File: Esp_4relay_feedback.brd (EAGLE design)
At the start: 150 x 100 mm, 93 parts, among them IC1 LM1117MP-3.3, IC2 NE555, IC4 7805TV, K1 G5LE, K2 G5LE, K3 G5LE, K4 G5LE, K5 G5LE, K6 G5LE, K7 G5LE, K8 G5LE, Q1 16MHz, Q11 BC450, Q2 BC547, Q3 BC547, Q4 BC547, Q5 BC547, Q6 BC547, Q7 BC547, Q8 BC547, Q9 BC547, T1 2N7000, T2 2N7000, U2 ATMEGA328P_PDIP

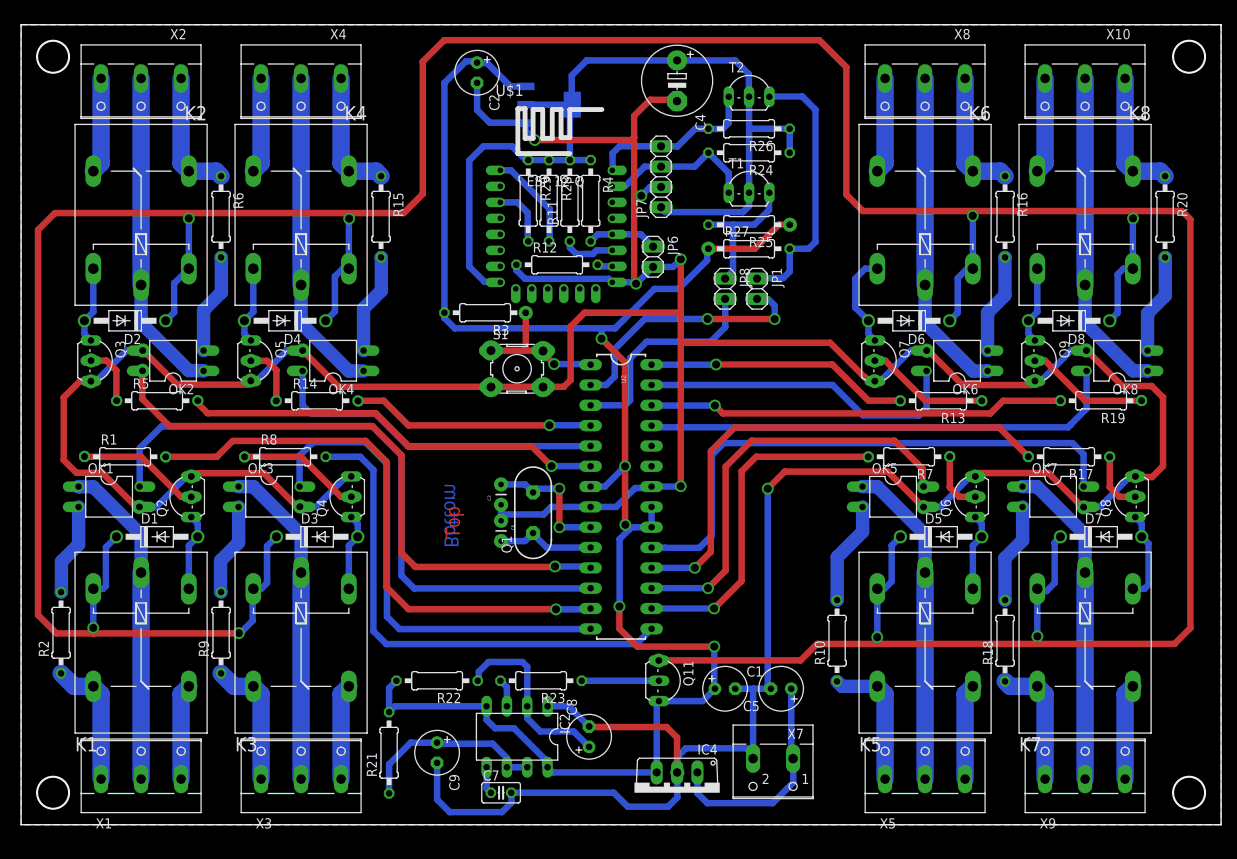
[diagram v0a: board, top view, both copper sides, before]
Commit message: schematic change
feedback circuit connection changed
added tip127 to control relay power supply.
made separate supply for relay and controller.
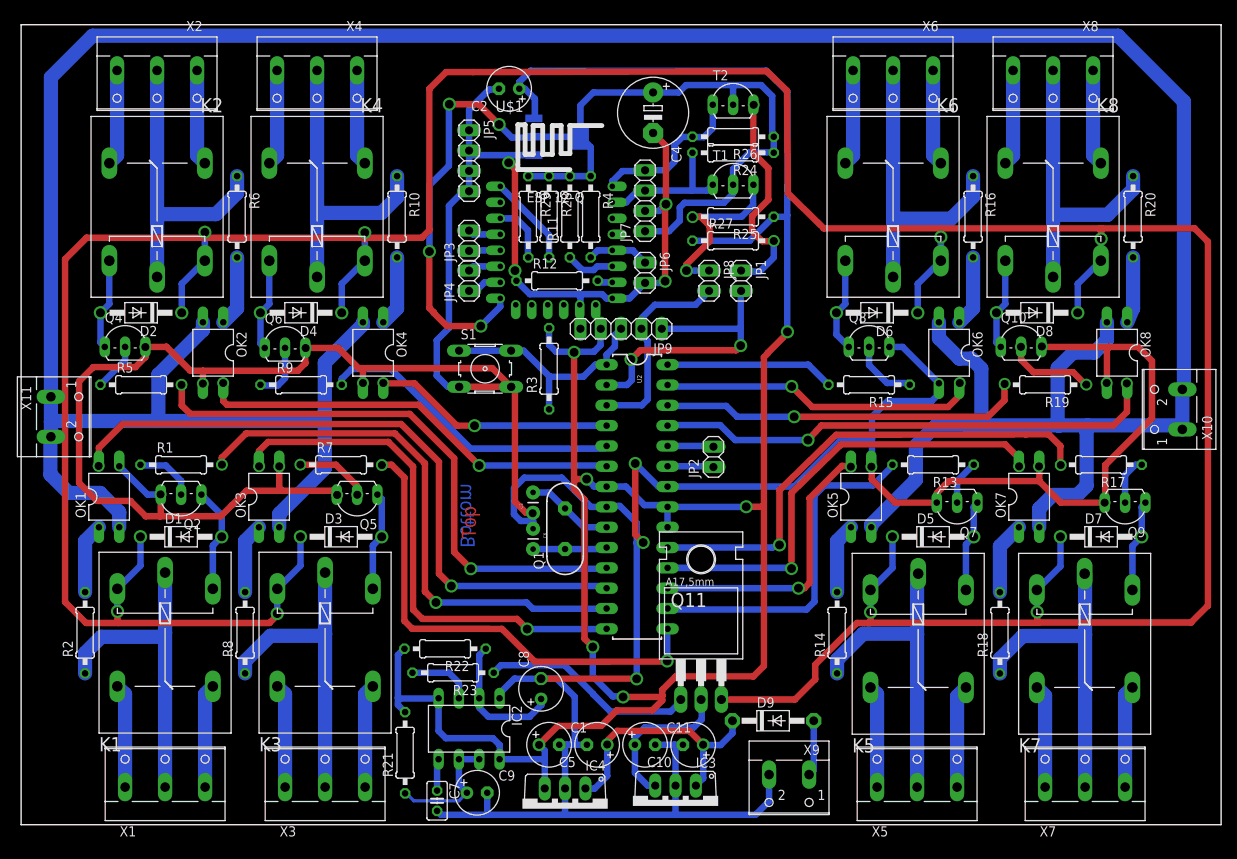
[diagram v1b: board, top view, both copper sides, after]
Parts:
- removed Q3: BC547, transistor-npn:TO92-EBC
- added C10, C11: 10uf, rcl:E2,5-6
- added D9: 1N4004, amit_diode_1N4004:DO41-10
- added IC3: 7805TV, linear:TO220V
- added JP2, JP3, JP4: (no value), pinhead:1X02
- added JP5: (no value), pinhead:1X04
- added JP9: (no value), pinhead:1X05
- added Q10: BC547, transistor-npn:TO92-EBC
- added X11: (no value), amit_screw_terminal_23:W237-102
- added X6: (no value), con-wago-500:W237-103
- Q11: value BC450 -> TIP120; device transistor-pnp:TO92-EBC -> transistor-power:TO220AH
- R14, R8: value 1k -> 220k
- R15, R9: value 220k -> 1k
- X10: device con-wago-500:W237-103 -> amit_screw_terminal_23:W237-102
- X7: device con-wago-500:W237-102 -> con-wago-500:W237-103
- X9: device con-wago-500:W237-103 -> con-wago-500:W237-102
- moved Q6 87.3 mm to (129.0, 60.9), turned to 0 degrees
- moved R10 76.4 mm to (143.0, 76.0), turned to 270 degrees
- moved R14 71.2 mm to (198.0, 24.0), turned to 90 degrees
- moved R7 71.0 mm to (136.0, 45.0), turned to 0 degrees
- moved R15 64.5 mm to (202.0, 55.0), turned to 180 degrees
- moved X10 41.5 mm to (239.9, 51.9), turned to 90 degrees
- moved X7 39.0 mm to (229.0, 6.00), turned to 0 degrees
- moved Q8 37.7 mm to (202.0, 61.0), turned to 0 degrees
- moved X9 37.1 mm to (192.0, 5.00), turned to 180 degrees
- moved Q4 33.6 mm to (109.0, 61.0), turned to 0 degrees
- moved R9 32.6 mm to (131.0, 55.0), turned to 0 degrees
- moved C5 24.0 mm to (168.0, 10.0)
- moved C1 23.1 mm to (162.0, 10.0)
- moved R8 22.6 mm to (124.0, 24.0), turned to 90 degrees
- moved Q5 21.6 mm to (138.0, 40.0), turned to 180 degrees
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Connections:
- removed net N$12 (its old number): D2.A, K2.2, Q3.C
- removed net N$18 (its old number): D3.A, K3.2, Q4.C
- removed net N$33 (its old number): C5.+, IC4.1, X7.1
- removed net N$35 (its old number): Q6.B, R7.1
- removed net N$61: D8.A, K8.2, Q9.C
- removed net VCC: C1.+, C2.+, IC1.3, IC2.4, IC2.8, IC4.3, Q11.E, R21.2, R22.2, R25.1, R27.1, R3.2, U2.20, U2.21, U2.7
- new net 12V: C10.+, C5.+, D9.C, IC3.1, IC4.1
- new net LINE: OK1.2, OK2.2, OK3.2, OK4.2, OK5.2, OK6.2, OK7.2, OK8.2, X10.1, X10.2, X11.1, X11.2
- new net N$112: C11.+, IC3.3, Q11.C
- new net N$30: OK4.1, R10.2
- new net N$31: K5.P, R14.1, X5.2
- new net N$42: OK5.1, R14.2
- new net N$43: K6.P, R16.1, X6.2
- new net N$44: K6.S, X6.1
- new net N$45: Q8.B, R15.1
- new net N$50: K7.S, X7.1
- new net N$62: JP3.1, U$1.GPIO14
- new net N$66: D9.A, X9.1
- new net VCC1: C1.+, C2.+, IC1.3, IC2.4, IC2.8, IC4.3, JP9.4, R21.2, R22.2, R25.1, R27.1, R3.2, U2.20, U2.21, U2.7
- net ERT: now also JP2.1
- net F2: now also U2.6; no longer U2.11
- net F4: now also U2.4; no longer U2.5
- net F7: now also U2.18; no longer U2.19
- net GND: now also C10.-, C11.-, IC3.2, JP5.1, JP5.2, JP5.3, JP5.4, JP9.5, Q10.E, X9.2; no longer Q3.E, X7.2
- net N$1: now also R2.1; no longer OK1.1
- net N$11: now also D2.A, K2.2, Q4.C; no longer Q3.B, R5.1
- net N$13: now also OK2.1, R6.2; no longer K3.P, OK3.1, X3.2
- net N$14: now also K3.P, R8.1, X3.2; no longer K3.S, R9.1, X3.1
- net N$15: now also K3.S, X3.1; no longer OK3.2, R9.2
- net N$16: now also Q5.B, R7.1; no longer K5.P, OK5.1, X5.2
- net N$17: now also D3.A, K3.2, Q5.C; no longer Q4.B, R8.1
- net N$19: now also OK3.1, R8.2; no longer K4.P, OK4.1, X4.2
- net N$2: now also OK1.1; no longer OK1.2
- net N$20: now also K4.P, R10.1, X4.2; no longer K4.S, R15.1, X4.1
- net N$22: now also K4.S, X4.1; no longer OK4.2, R15.2
- net N$24: now also Q6.B, R9.1; no longer Q5.B, R14.1
- net N$25: now also Q6.C; no longer Q5.C
- net N$3: no longer R2.1
- net N$32: no longer R10.1
- net N$34: now also D5.A, K5.2, Q7.C; no longer OK5.2, R10.2
- net N$4: now also R6.1; no longer OK2.1
- net N$46: now also D6.A, K6.2, Q8.C; no longer D5.A, K5.2, Q6.C
- net N$47: now also K6.O, X6.3; no longer K6.P, OK6.1, X8.2
- net N$48: now also OK6.1, R16.2; no longer K6.S, R16.1, X8.1
- net N$49: now also K7.P, R18.1, X7.2; no longer OK6.2, R16.2
- net N$51: now also Q9.B, R17.1; no longer D6.A, K6.2, Q7.C
- net N$52: now also D7.A, K7.2, Q9.C; no longer K7.P, OK7.1, X9.2
- net N$53: now also K7.O, X7.3; no longer K7.S, R18.1, X9.1
- net N$54: now also OK7.1; no longer OK7.2
- net N$55: now also K8.P, R20.1, X8.2; no longer Q8.B, R17.1
- net N$56: now also K8.S, X8.1; no longer D7.A, K7.2, Q8.C
- net N$57: now also Q10.B, R19.1; no longer K8.P, OK8.1, X10.2
- net N$58: now also D8.A, K8.2, Q10.C; no longer K8.S, R20.1, X10.1
- net N$59: now also K8.O, X8.3; no longer OK8.2, R20.2
- net N$6: no longer R6.1
- net N$60: now also OK8.1, R20.2; no longer Q9.B, R19.1
- net N$63: now also JP3.2, U$1.GPIO16; no longer K6.O, X8.3
- net N$64: now also JP4.1, U$1.GPIO13; no longer K7.O, X9.3
- net N$65: now also JP4.2, U$1.GPIO12; no longer K8.O, X10.3
- net N$9: now also Q4.B, R5.1; no longer OK2.2, R6.2
- net R2: now also U2.11; no longer U2.6
- net R3: now also R7.2; no longer R8.2
- net R4: now also R9.2, U2.5; no longer R14.2, U2.4
- net R5: now also R13.2; no longer R7.2
- net R6: now also R15.2; no longer R13.2
- net R7: now also U2.19; no longer U2.18
- net RELAY_SUPPLY: now also Q11.E; no longer Q11.C
- net RESET: now also JP9.3
- net RX: now also JP9.1
- net TX: now also JP9.2
- net WE: now also JP2.2
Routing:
- net LINE: track 0.00 -> 427.7 mm
- net VCC1: track 0.00 -> 290.2 mm, vias 0 -> 6
- net VCC: track 220.0 -> 0.00 mm, vias 5 -> 0
- net N$31: track 0.00 -> 39.8 mm
- net N$43: track 0.00 -> 39.6 mm
- net RELAY_SUPPLY: track 496.0 -> 457.6 mm
- net 12V: track 0.00 -> 32.4 mm
- net N$19: track 40.9 -> 8.83 mm
- net N$13: track 40.9 -> 8.83 mm
- net N$16: track 40.9 -> 9.27 mm
- net N$55: track 7.49 -> 38.9 mm, vias 1 -> 0
- net GND: track 529.0 -> 560.3 mm, vias 10 -> 9
- net N$57: track 40.9 -> 11.0 mm
- net N$52: track 40.9 -> 11.6 mm
- net N$47: track 40.9 -> 12.0 mm
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- removed copper zone on layer 16, net N$42
- removed copper zone on layer 1, net N$43
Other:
- outline, holes or cut-outs redrawn

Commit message: PDF
final pdf added.
developed PCB with this design
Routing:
- net RELAY_SUPPLY: track 457.6 -> 456.9 mm
- net GND: track 560.3 -> 559.8 mm
- added copper zone on layer 1, net N$105
- added copper zone on layer 16, net N$106
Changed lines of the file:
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@@
 <setting verticaltext="up"/>
 </settings>
-<grid distance="1" unitdist="mil" unit="mil" style="lines" multiple="1" display="yes" altdistance="1" altunitdist="mm" altunit="mm"/>
+<grid distance="1" unitdist="mm" unit="mm" style="lines" multiple="1" display="yes" altdistance="1" altunitdist="mm" altunit="mm"/>
 <layers>
-<layer number="1" name="Top" color="4" fill="1" visible="yes" active="yes"/>
+<layer number="1" name="Top" color="4" fill="1" visible="no" active="yes"/>
 <layer number="2" name="Route2" color="1" fill="3" visible="no" active="no"/>
 <layer number="3" name="Route3" color="4" fill="3" visible="no" active="no"/>
@@
 <layer number="17" name="Pads" color="2" fill="1" visible="yes" active="yes"/>
 <layer number="18" name="Vias" color="2" fill="1" visible="yes" active="yes"/>
-<layer number="19" name="Unrouted" color="6" fill="1" visible="yes" active="yes"/>
+<layer number="19" name="Unrouted" color="6" fill="1" visible="no" active="yes"/>
 <layer number="20" name="Dimension" color="15" fill="1" visible="yes" active="yes"/>
-<layer number="21" name="tPlace" color="7" fill="1" visible="yes" active="yes"/>
-<layer number="22" name="bPlace" color="7" fill="1" visible="yes" active="yes"/>
-<layer number="23" name="tOrigins" color="15" fill="1" visible="yes" active="yes"/>
-<layer number="24" name="bOrigins" color="15" fill="1" visible="yes" active="yes"/>
-<layer number="25" name="tNames" color="7" fill="1" visible="yes" active="yes"/>
-<layer number="26" name="bNames" color="7" fill="1" visible="yes" active="yes"/>
+<layer number="21" name="tPlace" color="7" fill="1" visible="no" active="yes"/>
+<layer number="22" name="bPlace" color="7" fill="1" visible="no" active="yes"/>
+<layer number="23" name="tOrigins" color="15" fill="1" visible="no" active="yes"/>
+<layer number="24" name="bOrigins" color="15" fill="1" visible="no" active="yes"/>
+<layer number="25" name="tNames" color="7" fill="1" visible="no" active="yes"/>
+<layer number="26" name="bNames" color="7" fill="1" visible="no" active="yes"/>
 <layer number="27" name="tValues" color="7" fill="1" visible="no" active="yes"/>
 <layer number="28" name="bValues" color="7" fill="1" visible="no" active="yes"/>
@@
 <wire x1="118.7196" y1="56.7436" x2="117.1702" y2="56.7436" width="0.8128" layer="1"/>
 <wire x1="122.3518" y1="39.9542" x2="120.9548" y2="38.5572" width="0.8128" layer="1"/>
-<wire x1="103.251" y1="55.4228" x2="105.029" y2="57.2008" width="0.8128" layer="1"/>
+<wire x1="103.7082" y1="55.9562" x2="105.029" y2="57.2008" width="0.8128" layer="1"/>
 <wire x1="105.029" y1="57.2008" x2="110.2868" y2="57.2008" width="0.8128" layer="1"/>
 <wire x1="110.2868" y1="57.2008" x2="111.5314" y2="58.4454" width="0.8128" layer="1"/>
@@
 <wire x1="111.5822" y1="38.5572" x2="109.6518" y2="40.4876" width="0.8128" layer="1"/>
 <wire x1="109.6518" y1="40.4876" x2="105.4862" y2="40.4876" width="0.8128" layer="1"/>
-<wire x1="105.4862" y1="40.4876" x2="103.251" y2="42.7228" width="0.8128" layer="1"/>
-<wire x1="103.251" y1="42.7228" x2="103.251" y2="55.4228" width="0.8128" layer="1"/>
+<wire x1="105.4862" y1="40.4876" x2="103.7082" y2="43.2562" width="0.8128" layer="1"/>
+<wire x1="103.7082" y1="43.2562" x2="103.7082" y2="55.9562" width="0.8128" layer="1"/>
 <wire x1="113.46" y1="41.27" x2="113.46" y2="38.8384" width="0.8128" layer="1"/>
 <wire x1="113.46" y1="38.8384" x2="113.4872" y2="38.8112" width="0.8128" layer="1"/>
@@
 <wire x1="138.938" y1="73.3806" x2="118.999" y2="73.3806" width="0.8128" layer="1"/>
 <wire x1="118.999" y1="73.3806" x2="104.1908" y2="73.3806" width="0.8128" layer="1"/>
-<wire x1="104.1908" y1="73.3806" x2="101.4984" y2="70.6882" width="0.8128" layer="1"/>
-<wire x1="101.4984" y1="70.6882" x2="101.4984" y2="27.8384" width="0.8128" layer="1"/>
-<wire x1="101.4984" y1="27.8384" x2="104.1146" y2="25.2222" width="0.8128" layer="1"/>
+<wire x1="104.1908" y1="73.3806" x2="102.3874" y2="71.5264" width="0.8128" layer="1"/>
+<wire x1="102.3874" y1="71.5264" x2="102.362" y2="27.051" width="0.8128" layer="1"/>
+<wire x1="102.362" y1="27.051" x2="104.1146" y2="25.2222" width="0.8128" layer="1"/>
 <wire x1="104.1146" y1="25.2222" x2="108.204" y2="25.2222" width="0.8128" layer="1"/>
 <wire x1="108.204" y1="25.2222" x2="127.0508" y2="25.2222" width="0.8128" layer="1"/>
@@
 <via x="183.5404" y="15.6718" extent="1-16" drill="1" diameter="1.4224" shape="square"/>
 </signal>
+<signal name="N$105">
+<polygon width="0.4064" layer="1" isolate="1.9304">
+<vertex x="96" y="100"/>
+<vertex x="246" y="100"/>
+<vertex x="246" y="0"/>
+<vertex x="96" y="0"/>
+</polygon>
+</signal>
+<signal name="N$106">
+<polygon width="0.4064" layer="16" isolate="1.9304">
+<vertex x="96" y="100"/>
+<vertex x="246" y="100"/>
+<vertex x="246" y="0"/>
+<vertex x="96" y="0"/>
+</polygon>
+</signal>
 </signals>

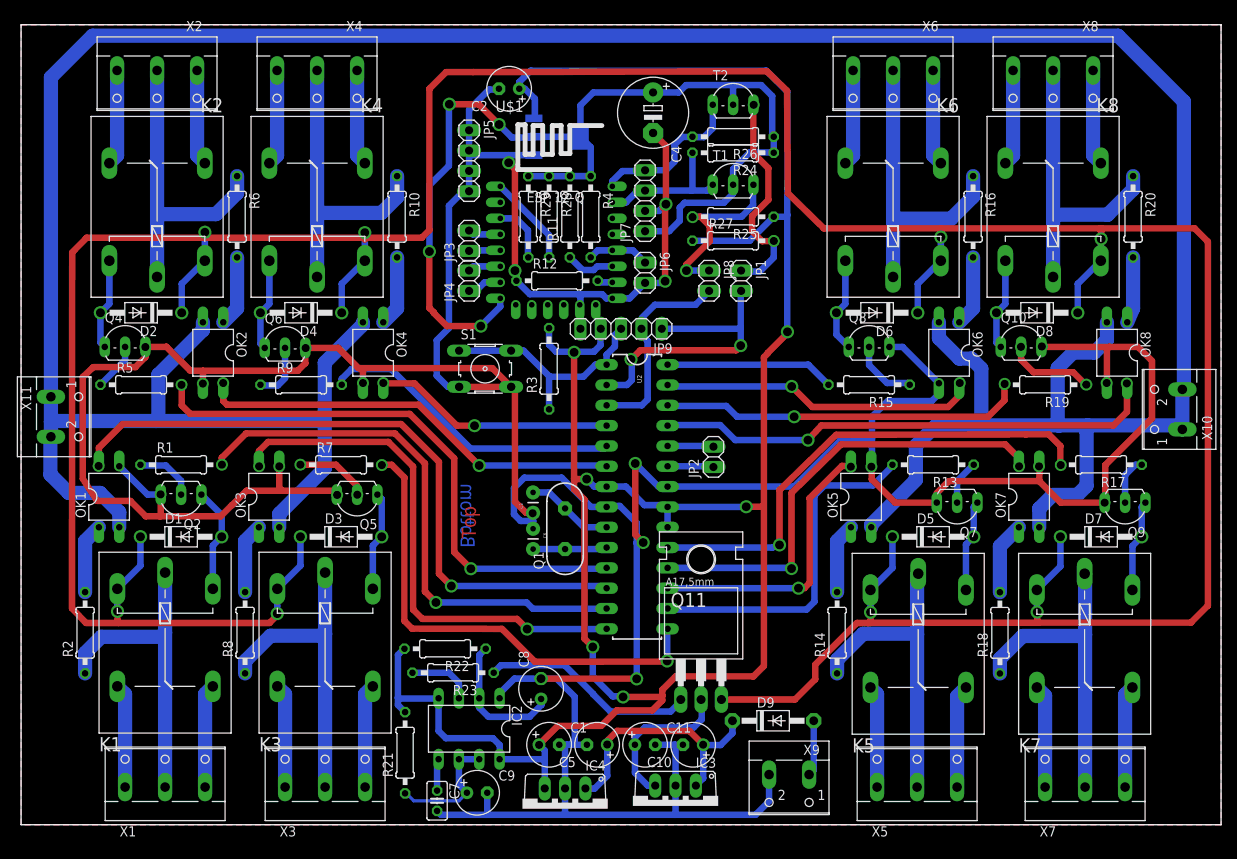
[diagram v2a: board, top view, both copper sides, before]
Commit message: schematic changes
EL814 pull up added.
HIGH LINK 5W supply added
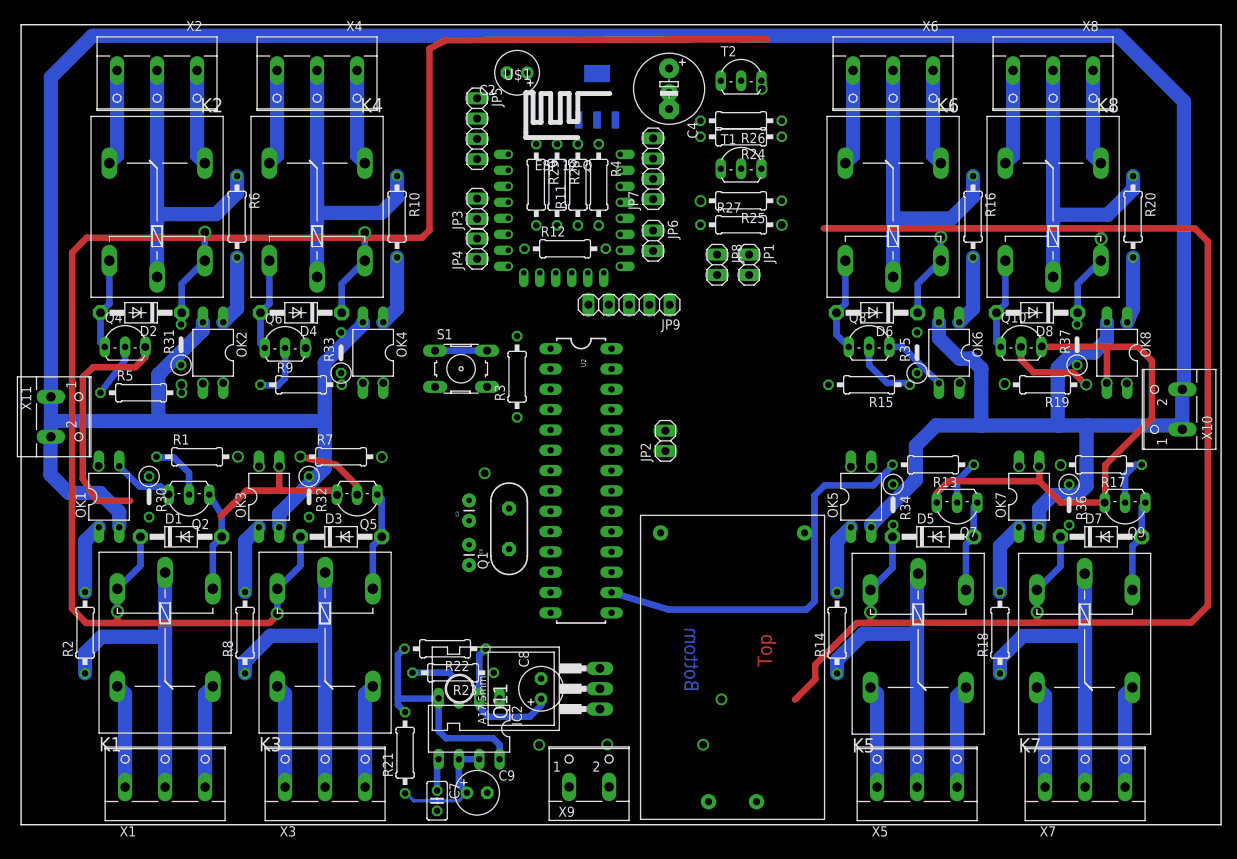
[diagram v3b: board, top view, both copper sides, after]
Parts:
- removed C1, C10, C11, C5: 10uf, rcl:E2,5-6
- removed D9: 1N4004, amit_diode_1N4004:DO41-10
- removed IC3, IC4: 7805TV, linear:TO220V
- added R30, R31, R32, R33, R34, R35, R36, R37: 10k, amit_rcl:0207/5V
- added U$2: AMIT_HIGH_LINK, amit_high_link_5W:AMIT_HIGH_LINK
- X9: device con-wago-500:W237-102 -> amit_screw_terminal_23:W237-102
- moved X9 25.0 mm to (167.0, 6.00), turned to 0 degrees
- moved Q11 19.6 mm to (162.0, 17.0), turned to 90 degrees
- moved C6 8.25 mm to (152.0, 35.0)
- moved C3 8.06 mm to (152.0, 38.0)
- moved U2 7.28 mm to (166.0, 43.0)
- moved IC1 7.07 mm to (168.0, 91.0), turned to 0 degrees
- moved Q1 7.00 mm to (157.0, 37.0)
- moved JP2 6.32 mm to (176.5, 48.0)
- moved JP3 4.12 mm to (153.0, 77.0)
- moved JP4 4.12 mm to (153.0, 72.0)
- moved JP5 4.12 mm to (153.0, 87.0)
- moved JP6 4.12 mm to (175.0, 73.0)
- moved JP7 4.12 mm to (175.0, 82.0)
- moved R11 4.12 mm to (165.6, 80.0)
- moved R12 4.12 mm to (164.0, 72.0)
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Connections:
- removed net 12V: C10.+, C5.+, D9.C, IC3.1, IC4.1
- removed net N$112: C11.+, IC3.3, Q11.C
- new net N$61: U$2.AC1, X9.1
- net F1: now also R30.1
- net F2: now also R31.1
- net F3: now also R32.1
- net F4: now also R33.1
- net F5: now also R34.1
- net F6: now also R35.1
- net F7: now also R36.1
- net F8: now also R37.1
- net GND: now also U$2.GND; no longer C1.-, C10.-, C11.-, C5.-, IC3.2, IC4.2, X9.2
- net N$66: now also U$2.AC2, X9.2; no longer D9.A, X9.1
- net RELAY_SUPPLY: now also Q11.C, R30.2, R31.2, R32.2, R33.2, R34.2, R35.2, R36.2, R37.2; no longer Q11.E
- net VCC1: now also Q11.E, U$2.VCC; no longer C1.+, IC4.3
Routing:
- net GND: track 559.8 -> 130.6 mm, vias 9 -> 2
- net VCC1: track 290.2 -> 28.0 mm, vias 6 -> 1
- net 3V3: track 132.5 -> 0.00 mm, vias 4 -> 0
- net F1: track 83.7 -> 0.00 mm, vias 1 -> 0
- net R2: track 71.0 -> 0.00 mm, vias 1 -> 0
- net R1: track 68.7 -> 0.00 mm, vias 1 -> 0
- net F3: track 66.0 -> 0.00 mm, vias 1 -> 0
- net F8: track 63.3 -> 0.00 mm, vias 1 -> 0
- net R7: track 61.8 -> 0.00 mm, vias 1 -> 0
- net R3: track 60.4 -> 0.00 mm, vias 1 -> 0
- net F7: track 57.6 -> 0.00 mm, vias 1 -> 0
- net F2: track 53.5 -> 0.00 mm, vias 1 -> 0
- net R8: track 45.5 -> 0.00 mm, vias 1 -> 0
- net F6: track 39.8 -> 0.00 mm, vias 1 -> 0
- net R4: track 38.6 -> 0.00 mm
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- removed copper zone on layer 1, net N$105
- removed copper zone on layer 16, net N$106
